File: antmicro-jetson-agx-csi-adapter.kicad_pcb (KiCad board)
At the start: 4 copper layers, 73.6 x 41 mm, 102 parts, among them IC1 MAX1708EEE+, J1 QTH-060-03-L-D-A, J2 WE_68715014522_ONE-SIDE, J3 WE_68715014022, J4 BM04B-SRSS-TB-LF-SN, J5 SM06B-SRSS-TB(LF)(SN), J6 SM09B-SRSS-TB(LF)(SN), Q1 BSS138AKA, U1 PCA9547BS,118, U2 NTS0102DP

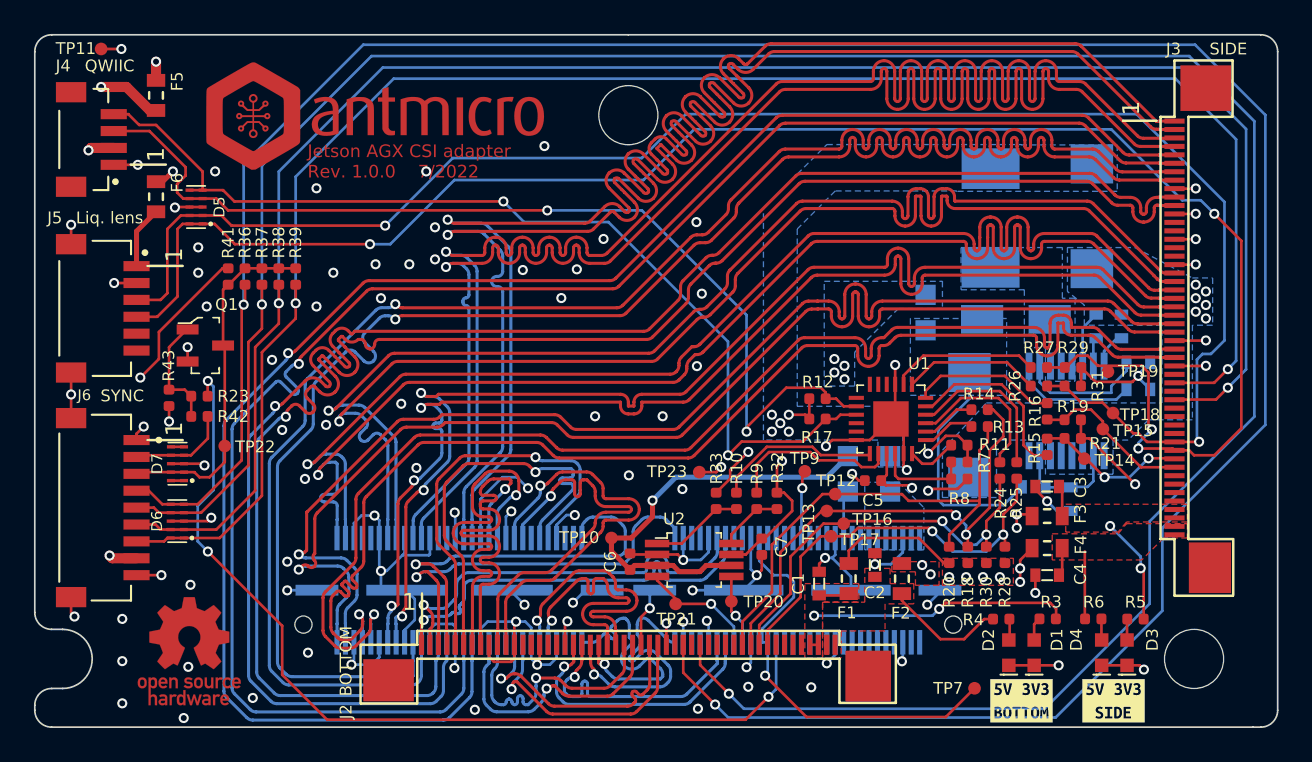
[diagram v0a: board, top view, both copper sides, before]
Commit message: Swapped QWIIC connector to a side entry one
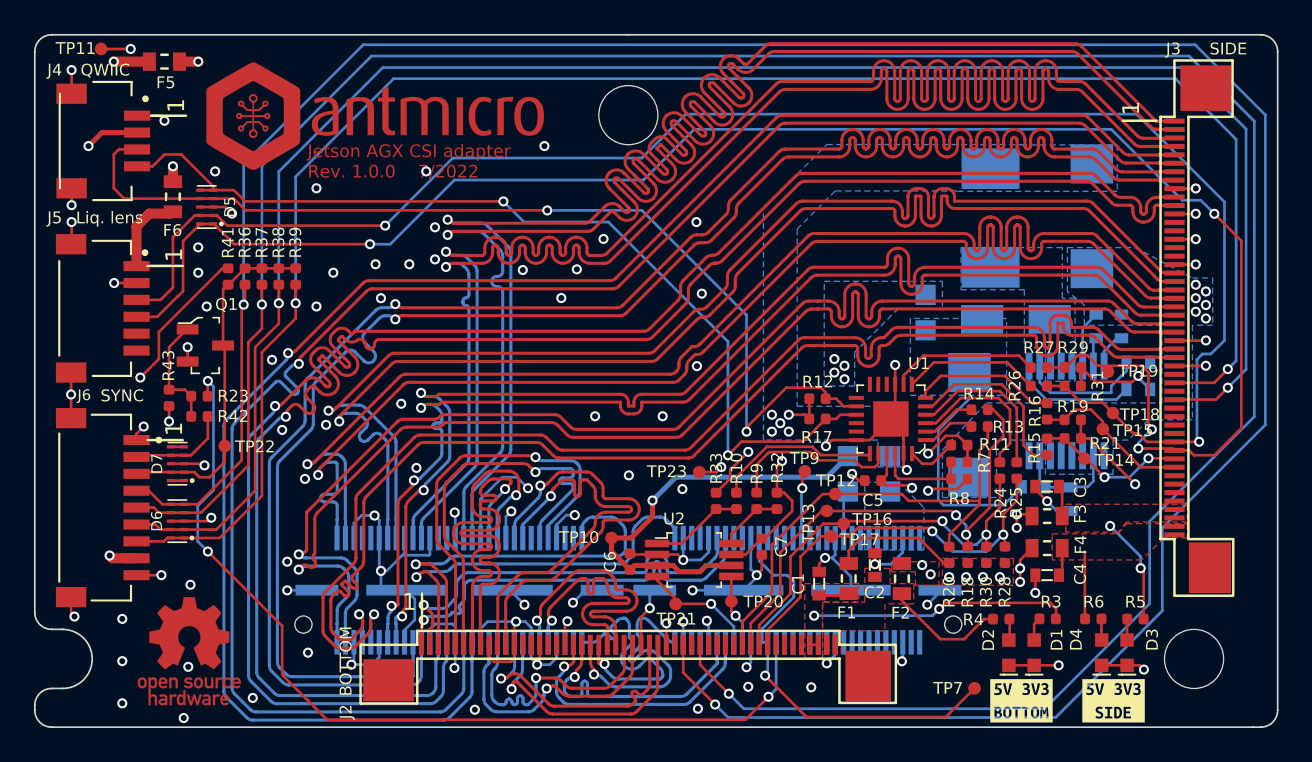
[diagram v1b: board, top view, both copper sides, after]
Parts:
- J4: value BM04B-SRSS-TB-LF-SN -> SM04B-SRSS-TB-LF-SN; footprint antmicro-footprints:BM04B-SRSS-TB-LF-SN -> antmicro-footprints:SM04B-SRSS-TB-LF-SN
- moved J4 2.71 mm to (120.9, 74.3), turned to -90 degrees
- moved F5 2.06 mm to (122.5, 69.6), turned to 0 degrees
- moved F6 1.00 mm to (123.0, 77.6)
- moved D5 0.63 mm to (125.0, 78.2)
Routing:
- net GND: track 146.0 -> 149.3 mm, vias 104 -> 106
- net /Auxiliary/AUX_I2C_SCL: track 58.7 -> 56.1 mm
- net /Auxiliary/5V_LL: track 3.70 -> 4.85 mm
- net CAM3_SCL: track 105.7 -> 105.0 mm
- net +3V3: track 54.8 -> 55.3 mm
- net /Auxiliary/AUX_I2C_SDA: track 58.9 -> 59.4 mm

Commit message: Fixed length matching
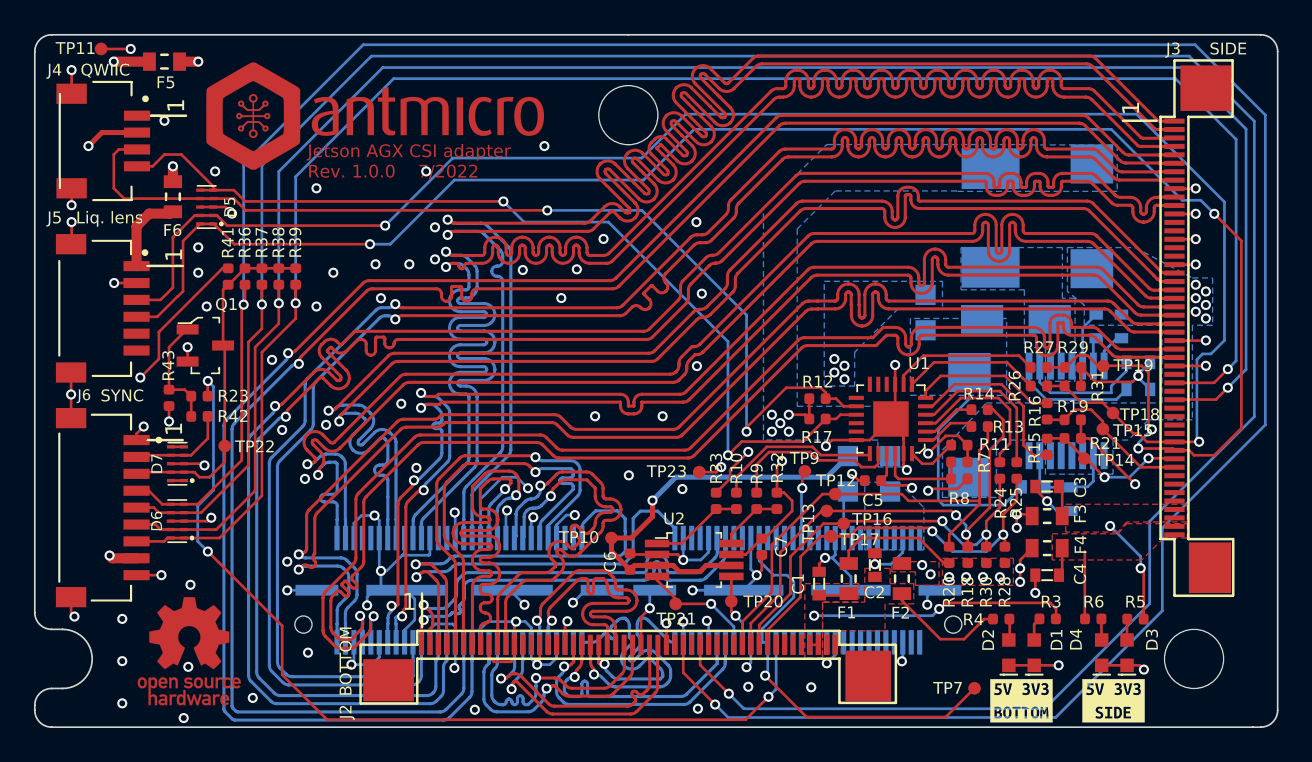
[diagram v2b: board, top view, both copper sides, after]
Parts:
- moved TP19 0.43 mm to (178.1, 87.7)
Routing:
- net GND: track 149.3 -> 152.1 mm, vias 106 -> 108
- net /Interface/CSI7_D0_N: track 23.1 -> 23.8 mm
- net /Interface/CSI7_D0_P: track 23.2 -> 23.9 mm
- net /Interface/CSI2_D1_N: track 99.9 -> 100.4 mm
- net /Interface/CSI2_D1_P: track 99.8 -> 100.4 mm
- net /Interface/CSI3_D1_P: track 99.4 -> 99.9 mm
- net /Interface/CSI3_D1_N: track 99.4 -> 100.0 mm

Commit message: Changed 5V converter capacitors to ceramic for lower ESR
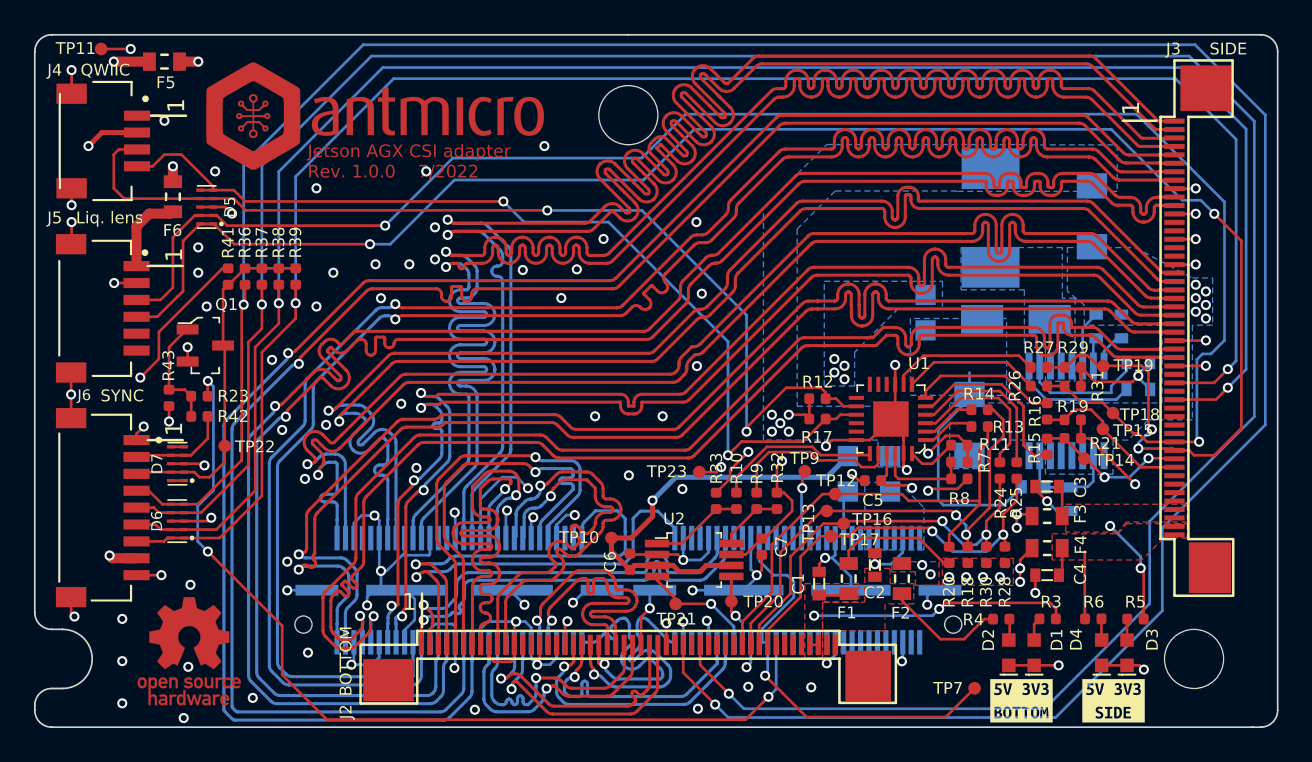
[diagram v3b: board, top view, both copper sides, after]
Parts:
- C12, C8: footprint antmicro-footprints:KEMET_D -> antmicro-footprints:1206-cap
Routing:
- net GND: track 152.1 -> 151.5 mm

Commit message: Fixed bottom silkscreen
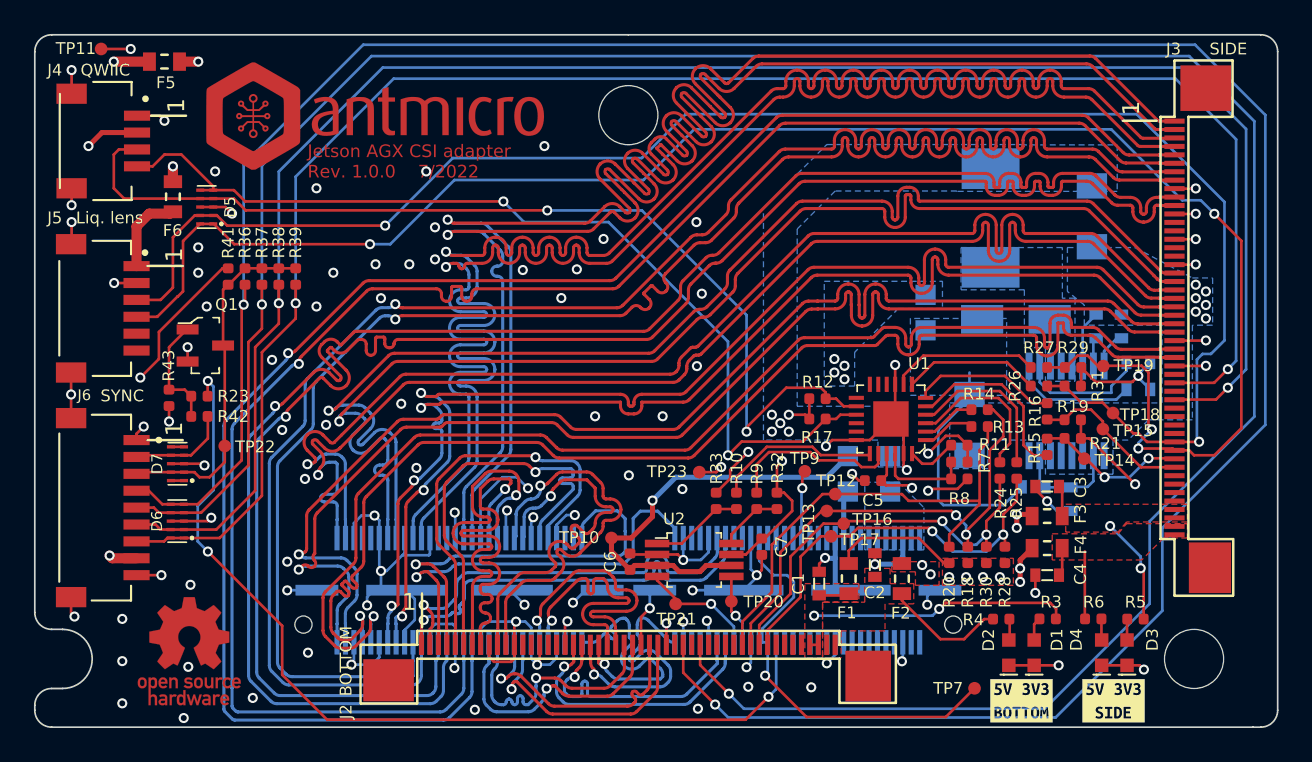
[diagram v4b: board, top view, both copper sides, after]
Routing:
- net GND: track 151.5 -> 152.1 mm

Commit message: Added loclib, updated README and added pdf schematic
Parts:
- C1, C10, C11, C2, C3, C4, C9: footprint antmicro-footprints:0603-cap -> antmicro-jetson-agx-csi-adapter-footprints:0603-cap
- C12, C8: footprint antmicro-footprints:1206-cap -> antmicro-jetson-agx-csi-adapter-footprints:1206-cap
- C5, C6, C7: footprint antmicro-footprints:0402-cap -> antmicro-jetson-agx-csi-adapter-footprints:0402-cap
- D1, D2, D3, D4: footprint antmicro-footprints:LED_0603 -> antmicro-jetson-agx-csi-adapter-footprints:LED_0603
- D5, D6, D7: footprint antmicro-footprints:PUSB3F96X -> antmicro-jetson-agx-csi-adapter-footprints:PUSB3F96X
- D8: footprint antmicro-footprints:DO-214AC -> antmicro-jetson-agx-csi-adapter-footprints:DO-214AC
- F1, F2, F3, F4, F5, F6: footprint antmicro-footprints:0603-Fuse-Littelfuse-0467 -> antmicro-jetson-agx-csi-adapter-footprints:0603-Fuse-Littelfuse-0467
- G***: footprint antmicro-footprints:antmicro-logo_scaled_20mm -> antmicro-jetson-agx-csi-adapter-footprints:antmicro-logo_scaled_20mm
- G***: footprint antmicro-footprints:oshw-logo -> antmicro-jetson-agx-csi-adapter-footprints:oshw-logo
- IC1: footprint antmicro-footprints:QSOP-16_3.9x4.9mm_P0.635mm -> antmicro-jetson-agx-csi-adapter-footprints:QSOP-16_3.9x4.9mm_P0.635mm
- J1: footprint antmicro-footprints:SAMTEC_QTH-060-03-X-D-A -> antmicro-jetson-agx-csi-adapter-footprints:SAMTEC_QTH-060-03-X-D-A
- J2: footprint antmicro-footprints:WE_68715014522_ONE-SIDE -> antmicro-jetson-agx-csi-adapter-footprints:WE_68715014522_ONE-SIDE
- J3: footprint antmicro-footprints:WE_68715014022 -> antmicro-jetson-agx-csi-adapter-footprints:WE_68715014022
- J4: footprint antmicro-footprints:SM04B-SRSS-TB-LF-SN -> antmicro-jetson-agx-csi-adapter-footprints:SM04B-SRSS-TB-LF-SN
- J5: footprint antmicro-footprints:JST_SM06B-SRSS-TB(LF)(SN) -> antmicro-jetson-agx-csi-adapter-footprints:JST_SM06B-SRSS-TB(LF)(SN)
- J6: footprint antmicro-footprints:JST_SM09B-SRSS-TB(LF)(SN) -> antmicro-jetson-agx-csi-adapter-footprints:JST_SM09B-SRSS-TB(LF)(SN)
- L1: footprint antmicro-footprints:IHLP2525CZER -> antmicro-jetson-agx-csi-adapter-footprints:IHLP2525CZER
- Q1: footprint antmicro-footprints:SOT-23-3 -> antmicro-jetson-agx-csi-adapter-footprints:SOT-23-3
- R1, R2, R22: footprint antmicro-footprints:0805-res -> antmicro-jetson-agx-csi-adapter-footprints:0805-res
- R10, R11, R12, R13, R14, R15, R16, R17, R18, R19, R20, R21, R23, R24, R25, R26, R27, R28, R29, R3, R30, R31, R32, R33, R36, R37, R38, R39, R4, R41, R42, R43, R5, R6, R7, R8, R9: footprint antmicro-footprints:0402-res -> antmicro-jetson-agx-csi-adapter-footprints:0402-res
- R34, R35, R40: footprint antmicro-footprints:0603-res -> antmicro-jetson-agx-csi-adapter-footprints:0603-res
- REF** (x2): footprint antmicro-footprints:mounting-hole-3.5mm-NPTH -> antmicro-jetson-agx-csi-adapter-footprints:mounting-hole-3.5mm-NPTH
- TP10, TP11, TP12, TP13, TP14, TP15, TP16, TP17, TP18, TP19, TP20, TP21, TP22, TP23, TP7, TP9: footprint antmicro-footprints:Testpoint_smd_0_75mm -> antmicro-jetson-agx-csi-adapter-footprints:Testpoint_smd_0_75mm
- U1: footprint antmicro-footprints:HVQFN24 -> antmicro-jetson-agx-csi-adapter-footprints:HVQFN24
- U2: footprint antmicro-footprints:TSSOP-8_W3mm -> antmicro-jetson-agx-csi-adapter-footprints:TSSOP-8_W3mm

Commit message: [#60956] WiP Update symbols references
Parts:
- C1, C10, C11, C2, C3, C4, C9: footprint antmicro-jetson-agx-csi-adapter-footprints:0603-cap -> antmicro-footprints:C_0603_1608Metric
- C12, C8: footprint antmicro-jetson-agx-csi-adapter-footprints:1206-cap -> antmicro-footprints:C_1206_3216Metric
- C5, C6, C7: footprint antmicro-jetson-agx-csi-adapter-footprints:0402-cap -> antmicro-footprints:C_0402_1005Metric
- D1, D2, D3, D4: footprint antmicro-jetson-agx-csi-adapter-footprints:LED_0603 -> antmicro-footprints:LED_0603_1608Metric_G
- D5, D6, D7: footprint antmicro-jetson-agx-csi-adapter-footprints:PUSB3F96X -> antmicro-footprints:Nexperia_DFN-10_2.5x1mm_P0.5mm
- F1, F2, F3, F4, F5, F6: footprint antmicro-jetson-agx-csi-adapter-footprints:0603-Fuse-Littelfuse-0467 -> antmicro-footprints:F_0603_1608Metric
- J1: footprint antmicro-jetson-agx-csi-adapter-footprints:SAMTEC_QTH-060-03-X-D-A -> antmicro-footprints:Conn_Plug_Samtec_QTH_2x60_QTH-060-03-L-D-A
- J5: footprint antmicro-jetson-agx-csi-adapter-footprints:JST_SM06B-SRSS-TB(LF)(SN) -> antmicro-footprints:Conn_JST_GH_1x6_SM06B-GHS-TB-LF-SN
- J6: footprint antmicro-jetson-agx-csi-adapter-footprints:JST_SM09B-SRSS-TB(LF)(SN) -> antmicro-footprints:Conn_JST_SH_1x9_SM09B-SRSS-TB-LF-SN
- L1: footprint antmicro-jetson-agx-csi-adapter-footprints:IHLP2525CZER -> antmicro-footprints:L_2525_6363Metric
- Q1: footprint antmicro-jetson-agx-csi-adapter-footprints:SOT-23-3 -> antmicro-footprints:SOT-23-3
- R1, R2, R22: footprint antmicro-jetson-agx-csi-adapter-footprints:0805-res -> antmicro-footprints:R_0805_2012Metric
- R10, R11, R12, R13, R14, R15, R16, R17, R18, R19, R20, R21, R23, R24, R25, R26, R27, R28, R29, R3, R30, R31, R32, R33, R36, R37, R38, R39, R4, R41, R42, R43, R5, R6, R7, R8, R9: footprint antmicro-jetson-agx-csi-adapter-footprints:0402-res -> antmicro-footprints:R_0402_1005Metric
- R34, R35, R40: footprint antmicro-jetson-agx-csi-adapter-footprints:0603-res -> antmicro-footprints:R_0603_1608Metric
- U1: footprint antmicro-jetson-agx-csi-adapter-footprints:HVQFN24 -> antmicro-footprints:VQFN-24-1EP_3.8x3.8x1.0mm_P0.5mm
- U2: footprint antmicro-jetson-agx-csi-adapter-footprints:TSSOP-8_W3mm -> antmicro-footprints:TSSOP-8_3x3mm_P0.65mm

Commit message: [#60956] WiP Update footprints
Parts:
- C10: value C_220n_0402 -> C_220n_0603
- C11, C9: value C_100n_0402 -> C_100n_0603
- C12, C8: value C_220u_KEMET_D -> C_220u_1206_6V3
- D1, D2, D3, D4: value LTST-C190GKT -> LED_G_0603_LTST-C190GKT
- F1, F2, F3, F4, F5, F6: value 04671.25NR -> F_1.25A_0603
- J1: value QTH-060-03-L-D-A -> Plug_Samtec_QTH_2x60_QTH-060-03-L-D-A
- J2: value WE_68715014522_ONE-SIDE -> Conn_FFC_WE_68715014522; footprint antmicro-jetson-agx-csi-adapter-footprints:WE_68715014522_ONE-SIDE -> antmicro-footprints:Conn_FFC_WE_68715014x22
- J3: value WE_68715014022 -> Conn_FFC_WE_68715014022_CUSTOM_FLIPPED; footprint antmicro-jetson-agx-csi-adapter-footprints:WE_68715014022 -> antmicro-footprints:Conn_FFC_WE_68715014x22_CUSTOM_FLIPPED
- J4: value SM04B-SRSS-TB-LF-SN -> JST_SH_1x4_SM04B-SRSS-TB-LF-SN; footprint antmicro-jetson-agx-csi-adapter-footprints:SM04B-SRSS-TB-LF-SN -> antmicro-footprints:Conn_JST_SH_1x4_SM04B-SRSS-TB-LF-SN
- J5: value SM06B-SRSS-TB(LF)(SN) -> JST_GH_1x6_SM06B-GHS-TB-LF-SN
- J6: value SM09B-SRSS-TB(LF)(SN) -> JST_SH_1x9_SM09B-SRSS-TB-LF-SN
- L1: value IHLP2525CZER2R2M01 -> L_8u2_4A_2525
- R34, R35: value R_2k_0402 -> R_2k2_0603
- R40: value R_2R_0402 -> R_2R_0603
- U1: value PCA9547BS,118 -> PCA9547_VQFN
- U2: value NTS0102DP -> NTS0102_TSSOP
- moved J2 2.75 mm to (150.0, 106.3)
- moved J4 2.17 mm to (118.7, 74.3)
- moved J3 1.62 mm to (184.5, 85.4), turned to 90 degrees
- turned C10 to 90 degrees
- turned C11 to 90 degrees
- turned C12 to 90 degrees
- turned C5 to 0 degrees
- turned C6 to -90 degrees
- turned C7 to 90 degrees
- turned C8 to 90 degrees
- turned C9 to -90 degrees
- turned D1 to -90 degrees
- turned D2 to -90 degrees
- turned D3 to -90 degrees
- turned D4 to -90 degrees
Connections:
- C10 pad 1: GND -> Net-(IC1-REF)
- C10 pad 2: Net-(C10-Pad2) -> GND
- C11 pad 1: Net-(C11-Pad1) -> GND
- C11 pad 2: GND -> Net-(IC1-CLK)
- C12 pad 1: /Auxiliary/5V_C -> GND
- C12 pad 2: GND -> /Auxiliary/5V_C
- C5 pad 1: +3V3 -> GND
- C5 pad 2: GND -> +3V3
- C6 pad 1: +1V8 -> GND
- C6 pad 2: GND -> +1V8
- C7 pad 1: +3V3 -> GND
- C7 pad 2: GND -> +3V3
- C8 pad 1: +3V3 -> GND
- C8 pad 2: GND -> +3V3
- C9 pad 1: Net-(C9-Pad1) -> GND
- C9 pad 2: GND -> Net-(IC1-SS/LIM)
- D1 pad 1: Net-(D1-Pad1) -> GND
- D1 pad 2: GND -> Net-(D1-A)
- D2 pad 1: Net-(D2-Pad1) -> GND
- D2 pad 2: GND -> Net-(D2-A)
- D3 pad 1: Net-(D3-Pad1) -> GND
- D3 pad 2: GND -> Net-(D3-A)
- D4 pad 1: Net-(D4-Pad1) -> GND
- D4 pad 2: GND -> Net-(D4-A)
- IC1 pad 10: Net-(C11-Pad1) -> Net-(IC1-CLK)
- IC1 pad 15: Net-(C11-Pad1) -> Net-(IC1-CLK)
- IC1 pad 16: Net-(C11-Pad1) -> Net-(IC1-CLK)
- IC1 pad 7: Net-(C9-Pad1) -> Net-(IC1-SS/LIM)
- IC1 pad 8: Net-(C10-Pad2) -> Net-(IC1-REF)
- J5 pad S1: GND -> (no net)
- J5 pad S2: GND -> (no net)
- J6 pad S1: GND -> (no net)
- J6 pad S2: GND -> (no net)
- R3 pad 2: Net-(D1-Pad1) -> Net-(D1-A)
- R4 pad 2: Net-(D2-Pad1) -> Net-(D2-A)
- R40 pad 1: Net-(C11-Pad1) -> Net-(IC1-CLK)
- R5 pad 2: Net-(D3-Pad1) -> Net-(D3-A)
- R6 pad 2: Net-(D4-Pad1) -> Net-(D4-A)
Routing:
- net GND: track 152.1 -> 162.9 mm, vias 108 -> 110
- net Net-(IC1-CLK): track 0.00 -> 7.08 mm
- net Net-(C11-Pad1): track 7.08 -> 0.00 mm
- net Net-(IC1-REF): track 0.00 -> 2.07 mm
- net Net-(C10-Pad2): track 1.96 -> 0.00 mm
- net Net-(IC1-SS/LIM): track 0.00 -> 1.48 mm
- net Net-(C9-Pad1): track 1.48 -> 0.00 mm
- net Net-(D1-Pad1): track 1.38 -> 0.00 mm
- net Net-(D1-A): track 0.00 -> 1.38 mm
- net Net-(D4-Pad1): track 1.23 -> 0.00 mm
- net Net-(D4-A): track 0.00 -> 1.23 mm
- net Net-(D3-Pad1): track 1.23 -> 0.00 mm
- net Net-(D3-A): track 0.00 -> 1.23 mm
- net Net-(D2-Pad1): track 1.23 -> 0.00 mm
- net Net-(D2-A): track 0.00 -> 1.23 mm
